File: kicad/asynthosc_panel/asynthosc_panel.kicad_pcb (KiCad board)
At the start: 2 copper layers, 71.1 x 128.4 mm, 24 parts, among them J15 Conn_02x04_Odd_Even

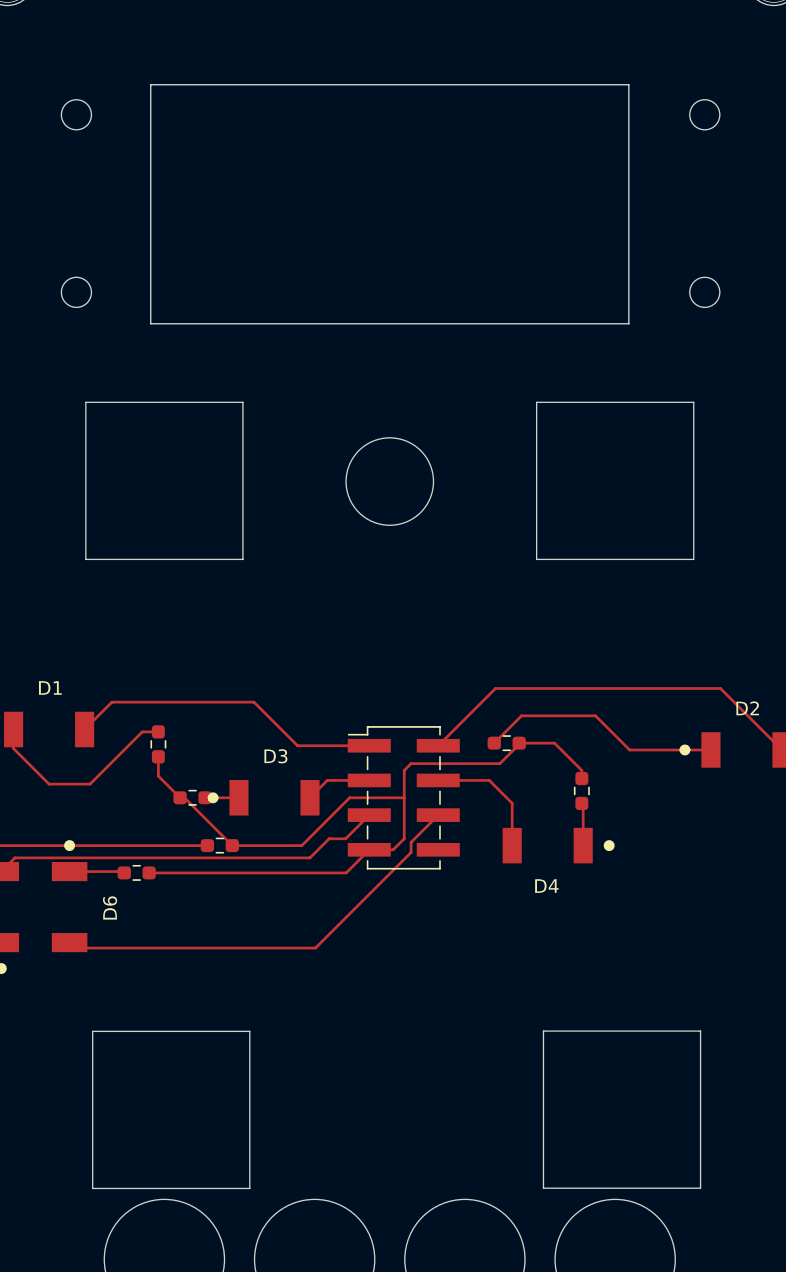
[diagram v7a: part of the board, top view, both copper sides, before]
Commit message: [PCB] Contours
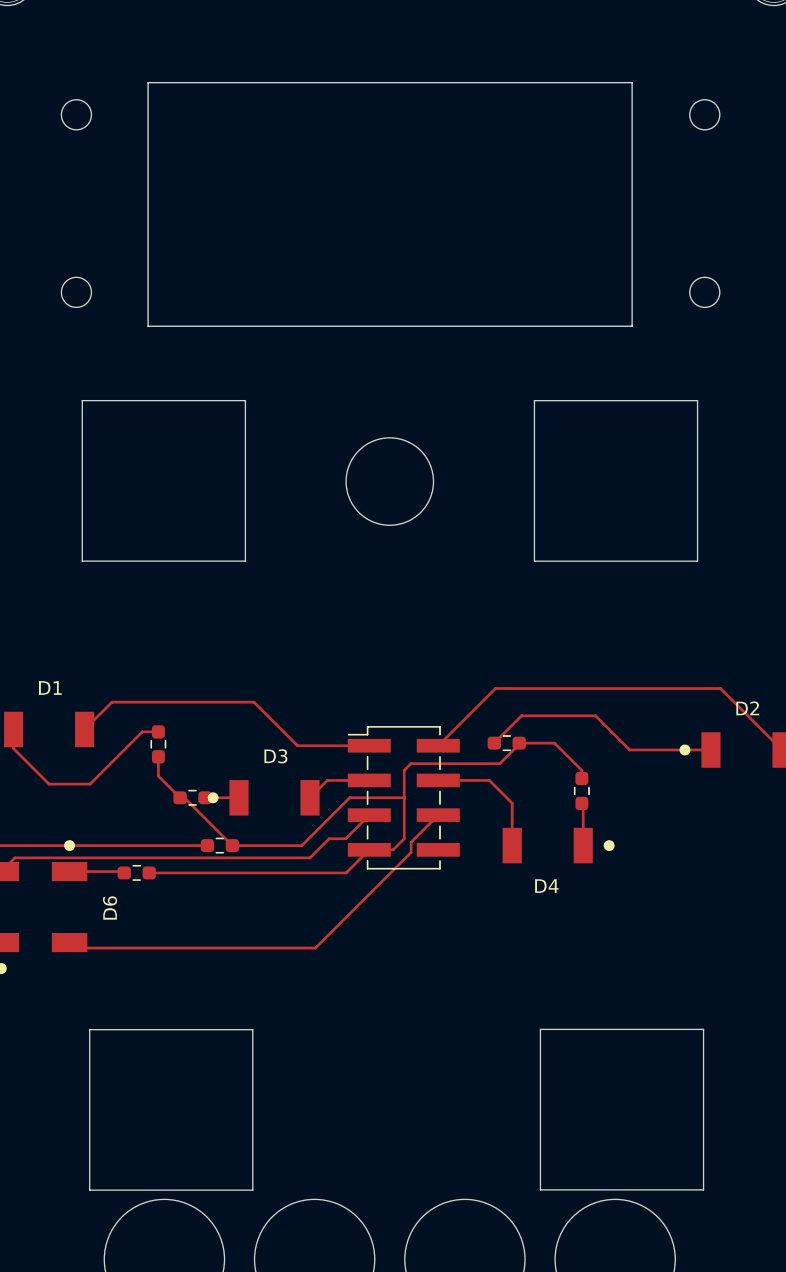
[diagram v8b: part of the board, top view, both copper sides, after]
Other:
- outline, holes or cut-outs redrawn
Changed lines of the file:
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@@
 	)
 	(gr_rect
-		(start 113.25 84.05)
-		(end 124.75 95.55)
+		(start 112.99 83.925)
+		(end 124.93 95.675)
+		(radius 0.5)
 		(stroke
 			(width 0.05)
@@
 		)
 		(fill no)
-		(locked yes)
 		(layer "Edge.Cuts")
 	)
 	(gr_rect
-		(start 113.75 130.1)
-		(end 125.25 141.6)
+		(start 113.53 129.975)
+		(end 125.47 141.725)
+		(radius 0.5)
 		(stroke
 			(width 0.05)
@@
 		)
 		(fill no)
-		(locked yes)
 		(layer "Edge.Cuts")
 	)
 	(gr_rect
-		(start 118 60.8)
-		(end 153 78.3)
+		(start 117.80582 60.647195)
+		(end 153.24 78.48)
+		(radius 0.5)
 		(stroke
 			(width 0.1)
@@
 		)
 		(fill no)
-		(locked yes)
 		(layer "Edge.Cuts")
 	)
@@
 	)
 	(gr_rect
-		(start 146.25 84.05)
-		(end 157.75 95.55)
+		(start 146.09 83.93)
+		(end 158.03 95.68)
+		(radius 0.5)
 		(stroke
 			(width 0.05)
@@
 		)
 		(fill no)
-		(locked yes)
 		(layer "Edge.Cuts")
 	)
 	(gr_rect
-		(start 146.75 130.08)
-		(end 158.25 141.58)
+		(start 146.53 129.955)
+		(end 158.47 141.705)
+		(radius 0.5)
 		(stroke
 			(width 0.05)
@@
 		)
 		(fill no)
-		(locked yes)
 		(layer "Edge.Cuts")
 	)
@@
 	)
 	(zone
+		(layer "F.Cu")
+		(hatch edge 0.5)
+		(connect_pads
+			(clearance 0)
+		)
+		(min_thickness 0.25)
+		(keepout
+			(tracks allowed)
+			(vias allowed)
+			(pads allowed)
+			(copperpour not_allowed)
+			(footprints allowed)
+		)
+		(placement
+			(enabled no)
+			(sheetname "")
+		)
+		(fill
+			(thermal_gap 0.5)
+			(thermal_bridge_width 0.5)
+			(island_removal_mode 0)
+		)
+		(polygon
+			(pts
+				(xy 128.56 109) (xy 145.56 109) (xy 145.56 115) (xy 128.56 115)
+			)
+		)
+	)
+	(zone
